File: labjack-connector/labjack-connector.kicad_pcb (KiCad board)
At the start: 2 copper layers, 19 x 58.7 mm, 2 parts, among them J1 connector, J2 DB37_Male

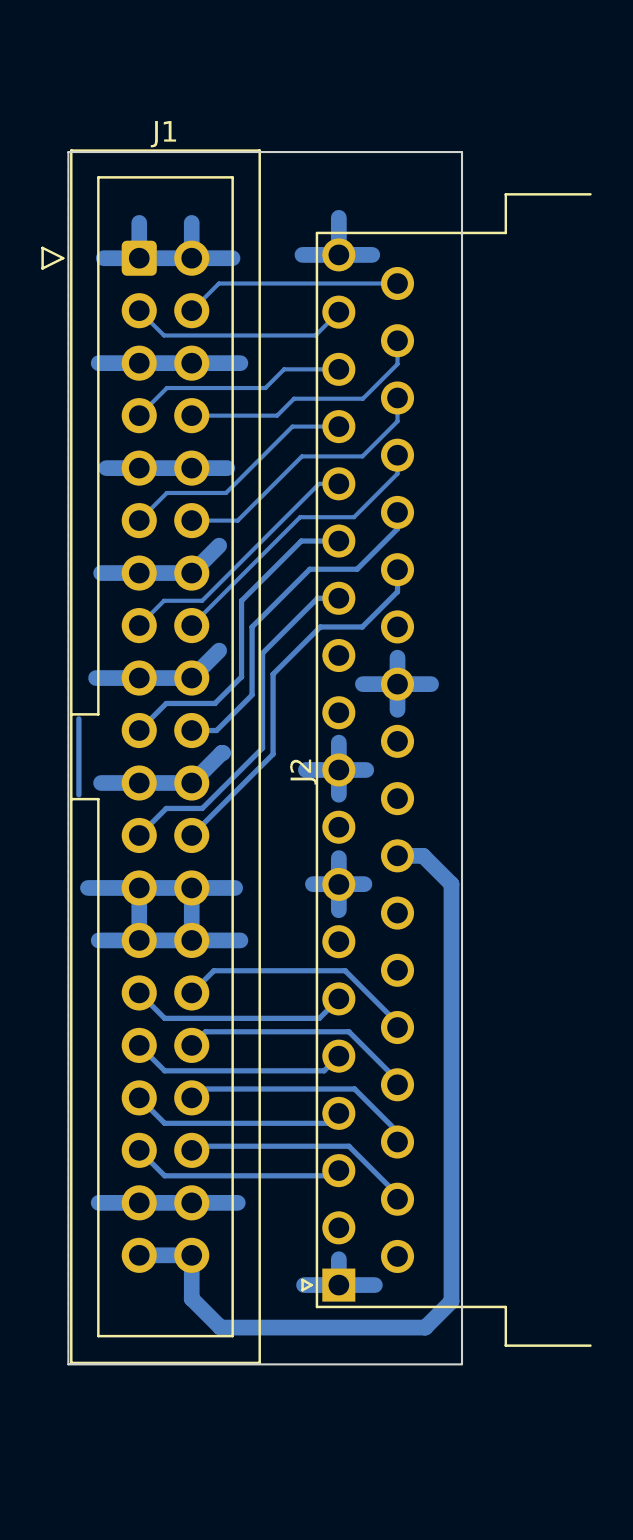
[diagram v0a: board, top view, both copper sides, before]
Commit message: Adjusted to OSH Park manufacturing
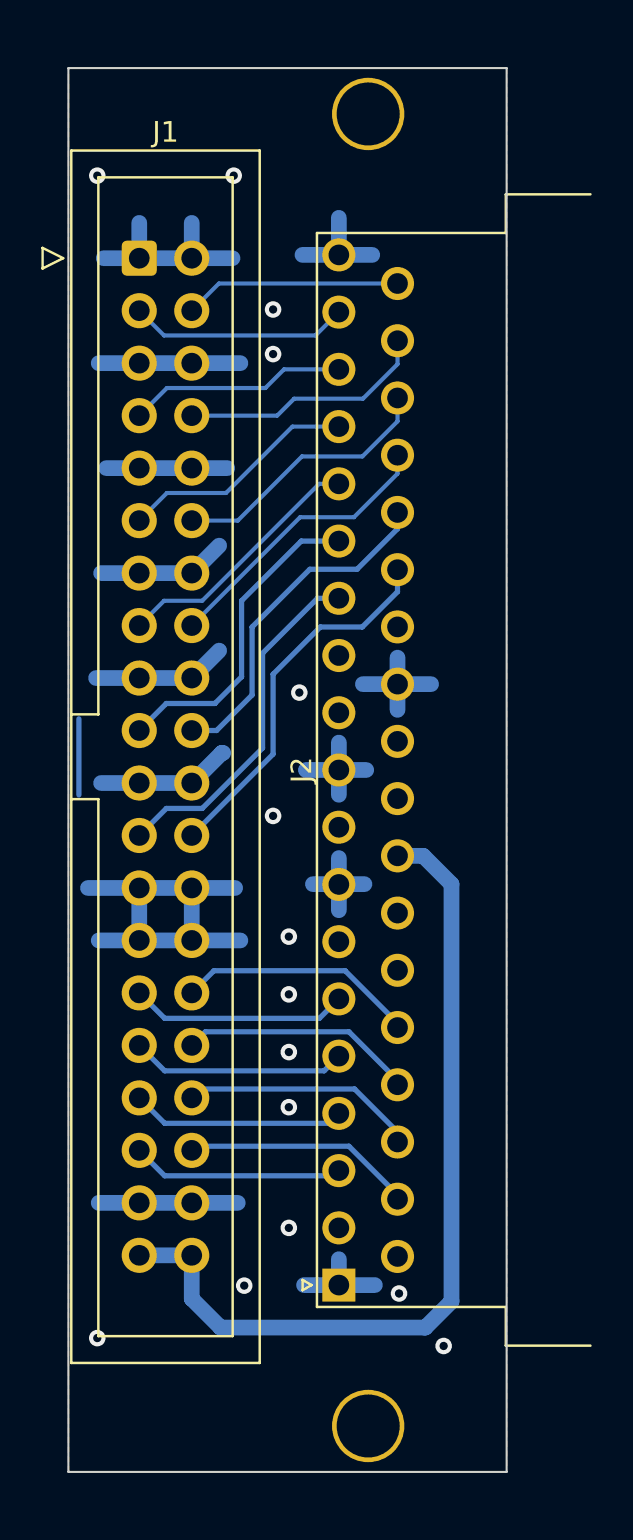
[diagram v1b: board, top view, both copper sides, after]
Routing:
- net GND: vias 0 -> 14
- net (no net): vias 0 -> 1
- added copper zone on F.Cu, net GND
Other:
- board size 19 x 58.7 mm -> 21.2 x 67.9 mm
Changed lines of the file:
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@@
   )
   (footprint "Connector_Dsub:DSUB-37_Male_Horizontal_P2.77x2.84mm_EdgePinOffset9.40mm" (layer "F.Cu")
-    (at 159.519669 109.575 90)
+    (at 159.519671 109.57499 90)
     (descr "37-pin D-Sub connector, horizontal/angled (90 deg), THT-mount, male, pitch 2.77x2.84mm, pin-PCB-offset 9.4mm, see http://docs-europe.electrocomponents.com/webdocs/1585/0900766b81585df2.pdf")
     (tags "37-pin D-Sub connector horizontal angled 90deg THT male pitch 2.77x2.84mm pin-PCB-offset 9.4mm")
@@
     (pad "37" thru_hole circle (at 48.475 2.84 90) (size 1.6 1.6) (drill 1) (layers *.Cu *.Mask)
       (net 3 "batt_0+") (pinfunction "37") (pintype "passive"))
+    (pad "mnt" thru_hole circle (at -6.82 1.42 90) (size 3.5 3.5) (drill 3.05) (layers *.Cu *.Mask))
+    (pad "mnt" thru_hole circle (at 56.68 1.42 90) (size 3.5 3.5) (drill 3.05) (layers *.Cu *.Mask))
+    (group "" (id aeaf6b90-ef71-4364-a504-89f59f1c73bd)
+      (members
+        4688c677-679c-42fe-9577-c31eda030fd5
+        5b5d8ca3-3873-40f7-8f07-03fdb321af66
+      )
+    )
     (model "${KICAD6_3DMODEL_DIR}/Connector_Dsub.3dshapes/DSUB-37_Male_Horizontal_P2.77x2.84mm_EdgePinOffset9.40mm.wrl"
       (offset (xyz 0 0 0))
@@
     )
   )
-  (gr_rect (start 165.481 113.411) (end 146.431 54.737) (layer "Edge.Cuts") (width 0.1) (fill none))
+  (gr_rect (start 167.64 118.618) (end 146.431 50.673) (layer "Edge.Cuts") (width 0.1) (fill none))
+  (via (at 156.337 62.357) (size 0.8) (drill 0.4) (layers "F.Cu" "B.Cu") (free) (net 0))
   (segment (start 146.939 82.169) (end 146.939 85.852) (width 0.254) (layer "B.Cu") (net 0))
+  (via (at 147.828 112.141) (size 0.8) (drill 0.4) (layers "F.Cu" "B.Cu") (free) (net 1))
+  (via (at 164.592 112.522) (size 0.8) (drill 0.4) (layers "F.Cu" "B.Cu") (free) (net 1))
+  (via (at 157.099 95.504) (size 0.8) (drill 0.4) (layers "F.Cu" "B.Cu") (free) (net 1))
+  (via (at 156.337 64.516) (size 0.8) (drill 0.4) (layers "F.Cu" "B.Cu") (free) (net 1))
+  (via (at 157.607 80.899) (size 0.8) (drill 0.4) (layers "F.Cu" "B.Cu") (free) (net 1))
+  (via (at 147.828 55.88) (size 0.8) (drill 0.4) (layers "F.Cu" "B.Cu") (free) (net 1))
+  (via (at 156.337 86.868) (size 0.8) (drill 0.4) (layers "F.Cu" "B.Cu") (free) (net 1))
+  (via (at 157.099 100.965) (size 0.8) (drill 0.4) (layers "F.Cu" "B.Cu") (free) (net 1))
+  (via (at 157.099 92.71) (size 0.8) (drill 0.4) (layers "F.Cu" "B.Cu") (free) (net 1))
+  (via (at 162.433 109.982) (size 0.8) (drill 0.4) (layers "F.Cu" "B.Cu") (free) (net 1))
+  (via (at 154.432 55.88) (size 0.8) (drill 0.4) (layers "F.Cu" "B.Cu") (free) (net 1))
+  (via (at 157.099 98.298) (size 0.8) (drill 0.4) (layers "F.Cu" "B.Cu") (free) (net 1))
+  (via (at 154.94 109.601) (size 0.8) (drill 0.4) (layers "F.Cu" "B.Cu") (free) (net 1))
+  (via (at 157.099 106.807) (size 0.8) (drill 0.4) (layers "F.Cu" "B.Cu") (free) (net 1))
   (segment (start 152.4 80.195) (end 153.728 78.867) (width 0.762) (layer "B.Cu") (net 1))
   (segment (start 149.86 90.355) (end 154.501 90.355) (width 0.762) (layer "B.Cu") (net 1))
@@
   (segment (start 162.359669 88.8) (end 163.603 88.8) (width 0.762) (layer "B.Cu") (net 22))
   (segment (start 152.4 108.135) (end 149.86 108.135) (width 0.762) (layer "B.Cu") (net 22))
+  (zone (net 1) (net_name "GND") (layer "F.Cu") (hatch edge 0.508)
+    (connect_pads (clearance 0.254))
+    (min_thickness 0.254) (filled_areas_thickness no)
+    (fill (thermal_gap 0.508) (thermal_bridge_width 0.508) (island_removal_mode 1) (island_area_min 0))
+    (polygon
+      (pts
+        (xy 167.64 118.618)
+        (xy 146.431 118.618)
+        (xy 146.431 50.673)
+        (xy 167.64 50.673)
+      )
+    )
+  )
   (zone (net 1) (net_name "GND") (layer "B.Cu") (hatch edge 0.508)
     (connect_pads no (clearance 0.254))
     (min_thickness 0.254) (filled_areas_thickness no)
-    (fill yes (thermal_gap 0.508) (thermal_bridge_width 0.508) (island_removal_mode 1) (island_area_min 0))
+    (fill (thermal_gap 0.508) (thermal_bridge_width 0.508))
     (polygon
       (pts
-        (xy 165.481 113.411)
-        (xy 146.431 113.411)
-        (xy 146.431 54.737)
-        (xy 165.481 54.737)
+        (xy 167.64 118.618)
+        (xy 146.431 118.618)
+        (xy 146.431 50.673)
+        (xy 167.64 50.673)
       )
     )

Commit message: LabJack<->test boards adapter board ready to go
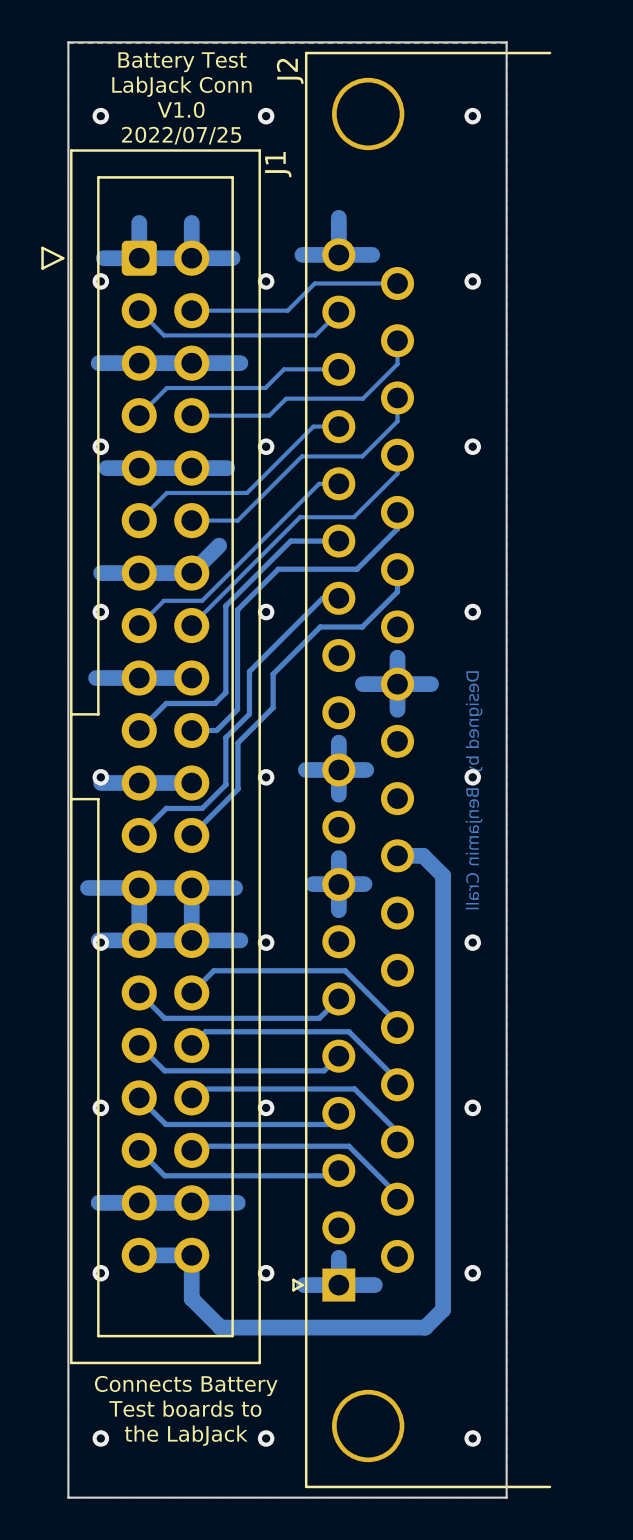
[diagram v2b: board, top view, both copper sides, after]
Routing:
- net GND: track 93.6 -> 89.7 mm, vias 14 -> 27
- net (no net): track 3.68 -> 0.00 mm, vias 1 -> 0
- net batt_0t: track 16.7 -> 17.6 mm
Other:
- board size 21.2 x 67.9 mm -> 21.2 x 70.4 mm
- board text added: "Battery Test LabJack Conn V1.0 2022/07/25"
- board text added: "Connects Battery Test boards to the LabJack"
- board text added: "Designed by Benjamin Crall"

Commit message: Added part number
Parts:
- J2: footprint Connector_Dsub:DSUB-37_Male_Horizontal_P2.77x2.84mm_EdgePinOffset9.40mm -> oresat-footprints:DSUB-37_Male_Horizontal_P2.77x2.84mm_MountingHoles
